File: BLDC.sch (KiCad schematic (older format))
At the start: 122 parts, among them J1 436500513, J2 436500313, J3 TC2030-MCP-NL, J4 436500513, U0 LSM6DS3US, U12 MCP9808, U13 AS5047D-ATSM, U17 INA250, U18 INA250, U19 INA250, U2 LM5166, U3 TLV702, U4 LM5166, U5 DRV8312, U6 ISL32458E, U7 SN74LVC1G66DCKR, U9 STM32F405RG

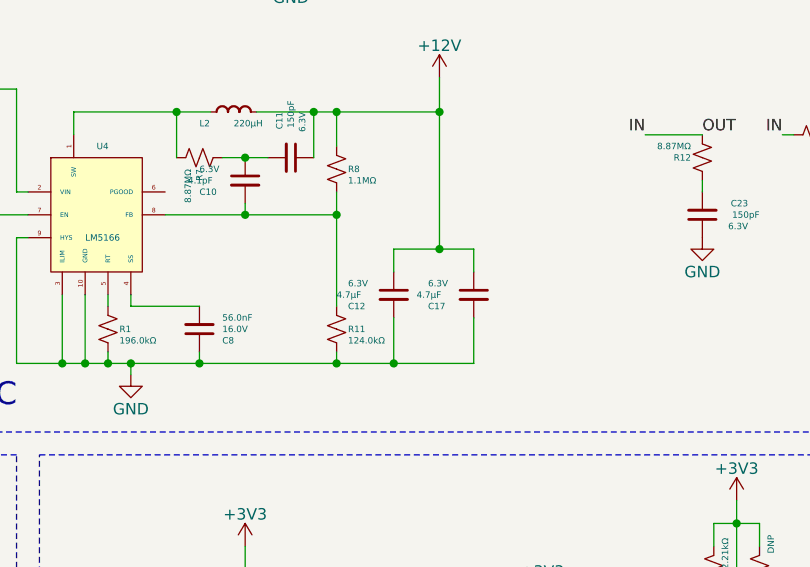
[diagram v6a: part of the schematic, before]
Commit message: Added ground pour in bottom layer for thermal dissipation and current return
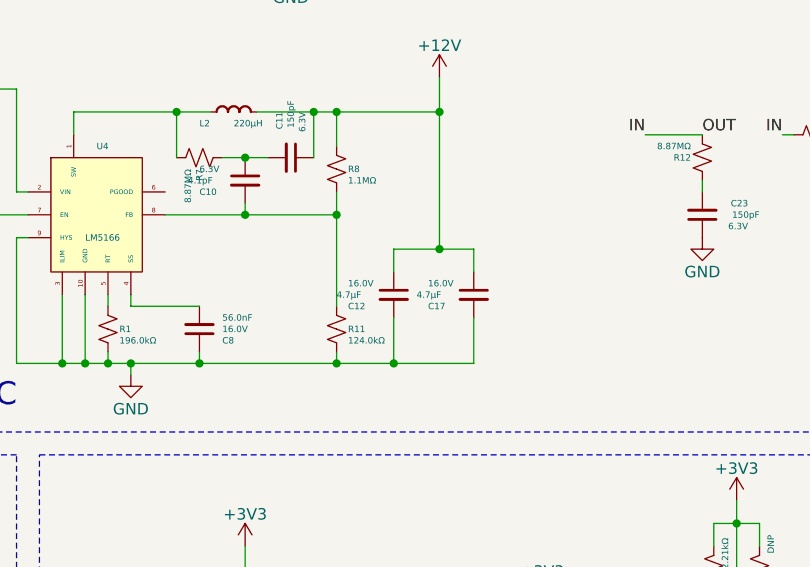
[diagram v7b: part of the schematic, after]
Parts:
- C12, C17: footprint Capacitor_SMD:C_1206_3216Metric -> Capacitor_SMD:C_0805_2012Metric; Maximum Voltage 6.3V -> 16.0V
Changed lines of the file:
@@
 EESchema Schematic File Version 5
 LIBS:BLDC-cache
-EELAYER 29 0
+EELAYER 30 0
 EELAYER END
 $Descr A3 16535 11693
@@
 F 0 "C12" H 8650 3850 28  0000 L CNN
 F 1 "4.7μF" H 8600 3900 28  0000 L CNN
-F 2 "Capacitor_SMD:C_1206_3216Metric" H 8850 3900 60  0001 C CNN
+F 2 "Capacitor_SMD:C_0805_2012Metric" H 8850 3900 60  0001 C CNN
 F 3 "" H 8850 3900 60  0001 C CNN
 F 4 "4.7μF" H 8850 3900 60  0001 C CNN "Capacitance"
 F 5 "40.0%" H 8850 3900 60  0001 C CNN "Tolerance"
-F 6 "6.3V" H 8650 3950 28  0000 L CNN "Maximum Voltage"
+F 6 "16.0V" H 8650 3950 28  0000 L CNN "Maximum Voltage"
 	1    8850 3900
 	1    0    0    -1
@@
 F 0 "C17" H 9000 3850 28  0000 L CNN
 F 1 "4.7μF" H 8950 3900 28  0000 L CNN
-F 2 "Capacitor_SMD:C_1206_3216Metric" H 9200 3900 60  0001 C CNN
+F 2 "Capacitor_SMD:C_0805_2012Metric" H 9200 3900 60  0001 C CNN
 F 3 "" H 9200 3900 60  0001 C CNN
 F 4 "4.7μF" H 9200 3900 60  0001 C CNN "Capacitance"
 F 5 "40.0%" H 9200 3900 60  0001 C CNN "Tolerance"
-F 6 "6.3V" H 9000 3950 28  0000 L CNN "Maximum Voltage"
+F 6 "16.0V" H 9000 3950 28  0000 L CNN "Maximum Voltage"
 	1    9200 3900
 	1    0    0    -1

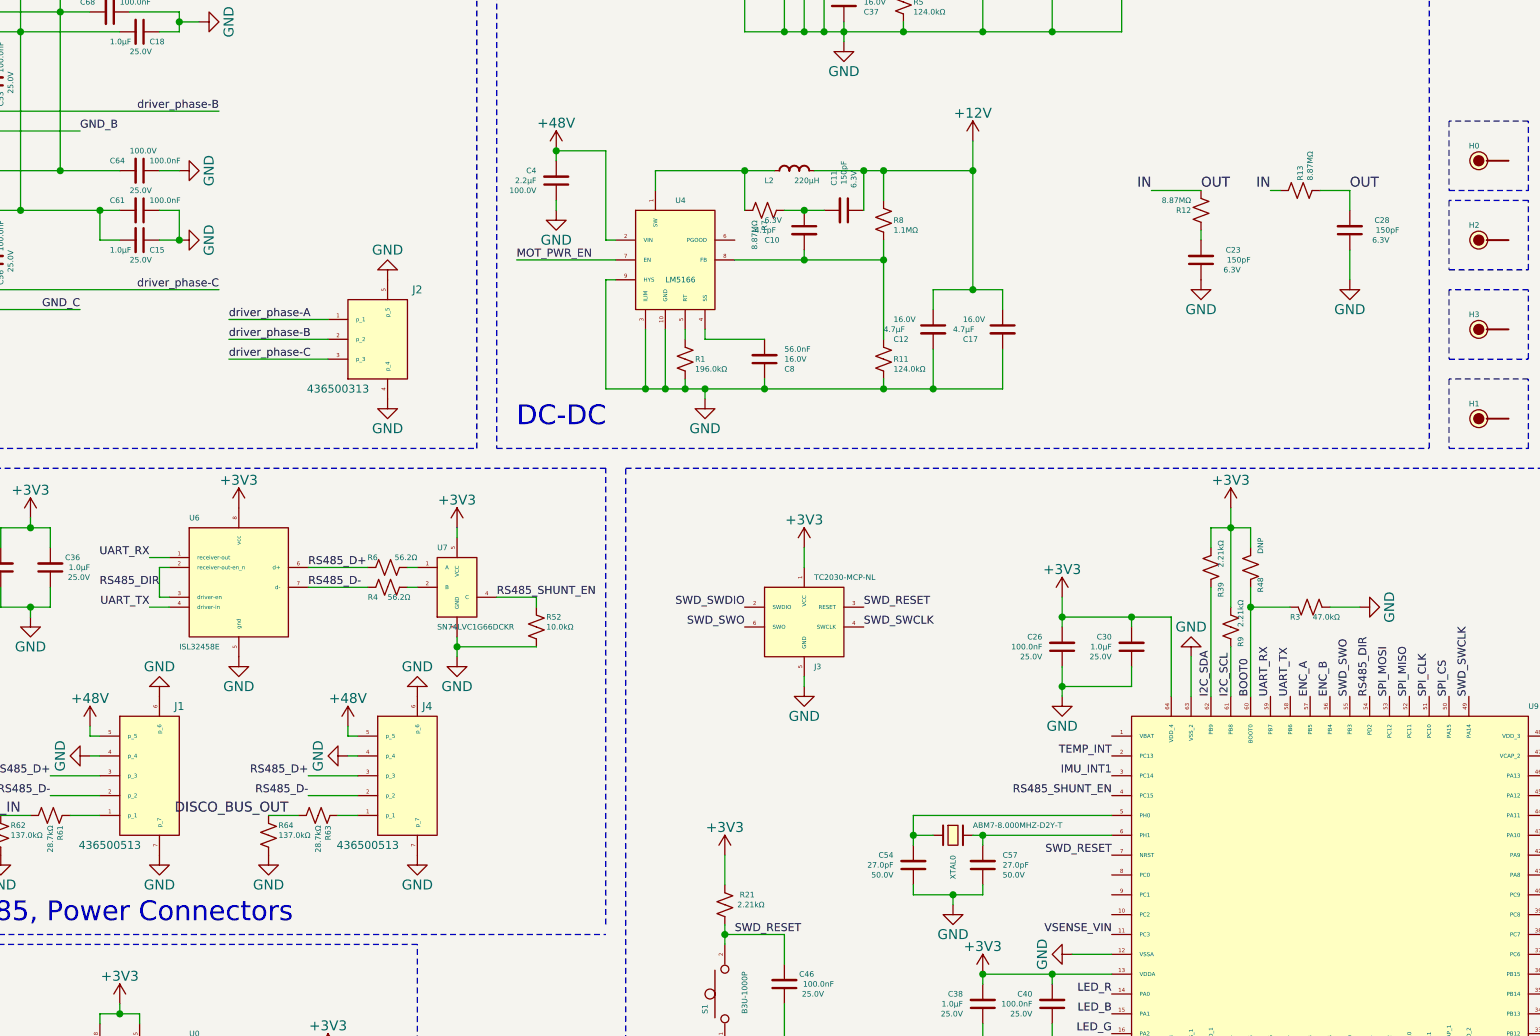
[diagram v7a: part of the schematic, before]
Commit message: Changed J1 connector to through hole and moved to middle of PCB
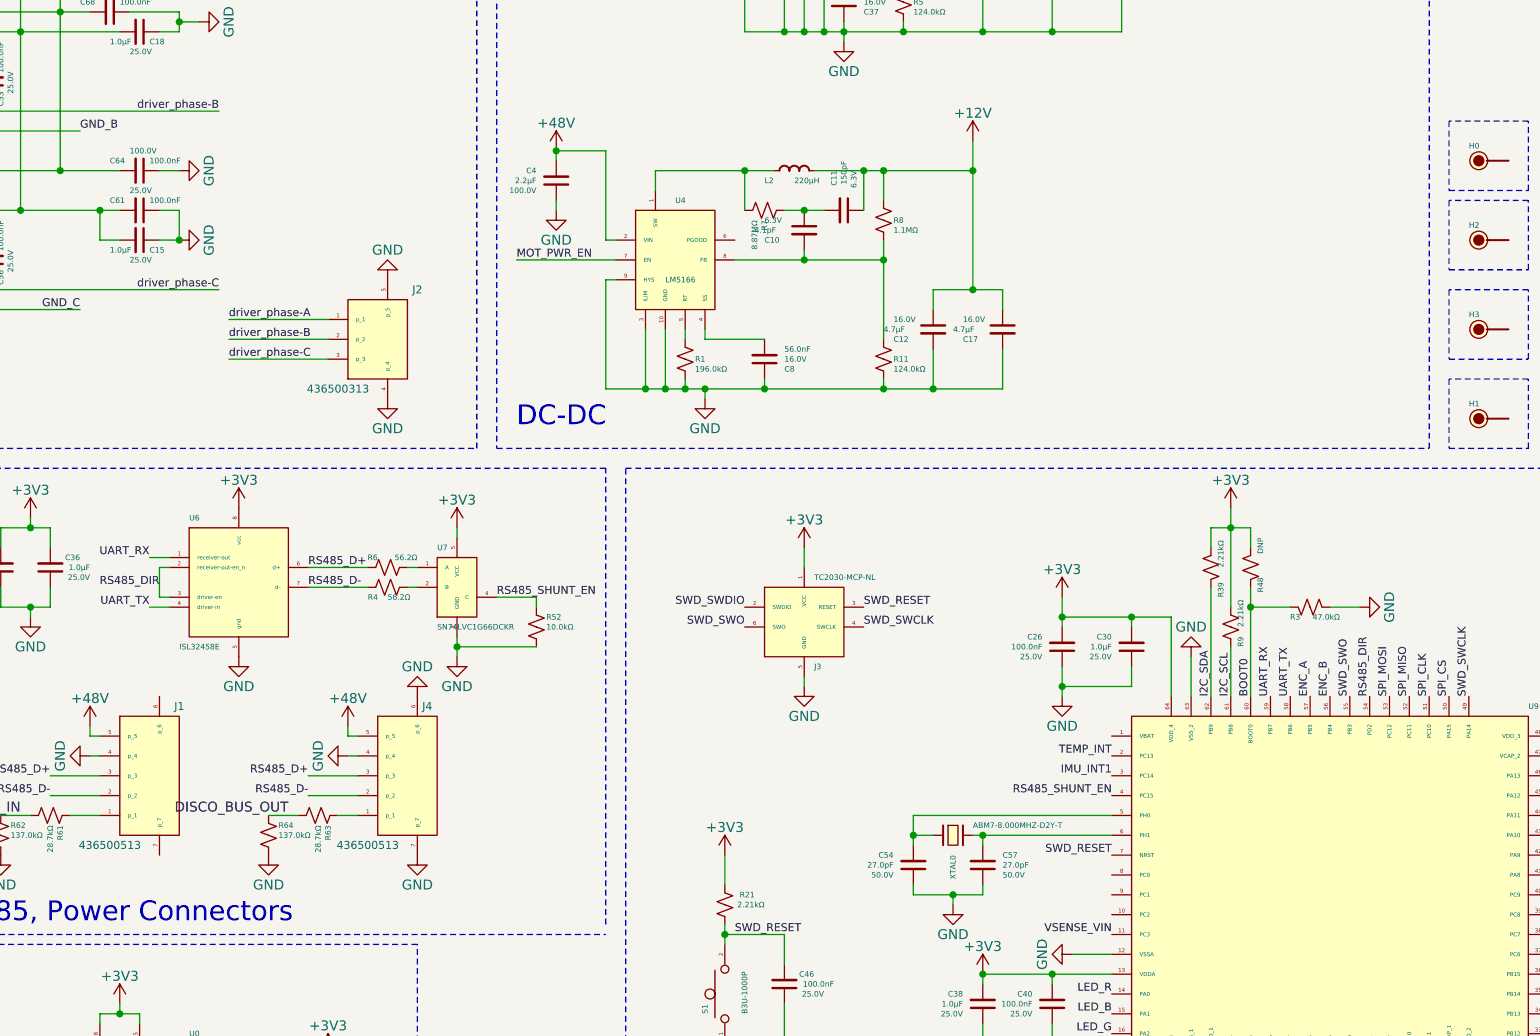
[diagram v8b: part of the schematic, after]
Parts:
- removed C23, C28: 150pF, Capacitor_SMD:C_0805_2012Metric, symbol Device:C_Small
- removed R12, R13: 8.87MΩ, Resistor_SMD:R_0805_2012Metric, symbol Device:R_Small_US
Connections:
- net GND: no longer J1.6 (p_6), J1.7 (p_7)
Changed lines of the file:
@@
-$EndComp
-$Comp
-L power:GND #PWR090
-U 1 1 5BCC0025
-P 4950 6550
-F 0 "#PWR090" H 4950 6300 50  0001 C CNN
-F 1 "GND" H 4950 6400 50  0000 C CNN
-F 2 "" H 4950 6550 50  0001 C CNN
-F 3 "" H 4950 6550 50  0001 C CNN
-	1    4950 6550
-	1    0    0    -1
 $EndComp
 $Comp
@@
 F 3 "" H 6250 5750 50  0001 C CNN
 	1    6250 5750
-	-1   0    0    1
-$EndComp
-$Comp
-L power:GND #PWR087
-U 1 1 5BCBFA49
-P 4950 5750
-F 0 "#PWR087" H 4950 5500 50  0001 C CNN
-F 1 "GND" H 4950 5600 50  0000 C CNN
-F 2 "" H 4950 5750 50  0001 C CNN
-F 3 "" H 4950 5750 50  0001 C CNN
-	1    4950 5750
 	-1   0    0    1
 $EndComp
@@
 $EndComp
 $Comp
-L Device:R_Small_US R12
-U 1 1 5D4F3434
-P 10200 3300
-F 0 "R12" H 10250 3300 28  0000 L CNN
-F 1 "8.87MΩ" H 10250 3250 28  0000 L CNN
-F 2 "Resistor_SMD:R_0805_2012Metric" H 10200 3300 60  0001 C CNN
-F 3 "" H 10200 3300 60  0001 C CNN
-F 4 "8870000.0ohm" H 10200 3300 60  0001 C CNN "Resistance"
-F 5 "0.1%" H 10200 3300 60  0001 C CNN "Tolerance"
-F 6 "0.125W" H 10200 3300 60  0001 C CNN "Maximum Power"
-	1    10200 3300
-	-1   0    0    1
-$EndComp
-$Comp
-L Device:C_Small C23
-U 1 1 5D4F868D
-P 10200 3550
-F 0 "C23" H 10000 3500 28  0000 L CNN
-F 1 "150pF" H 9950 3550 28  0000 L CNN
-F 2 "Capacitor_SMD:C_0805_2012Metric" H 10200 3550 60  0001 C CNN
-F 3 "" H 10200 3550 60  0001 C CNN
-F 4 "150pF" H 10200 3550 60  0001 C CNN "Capacitance"
-F 5 "40.0%" H 10200 3550 60  0001 C CNN "Tolerance"
-F 6 "6.3V" H 10000 3600 28  0000 L CNN "Maximum Voltage"
-	1    10200 3550
-	-1   0    0    1
-$EndComp
-Wire Wire Line
-	9950 3200 10200 3200
-Wire Wire Line
-	10200 3400 10200 3450
-$Comp
-L power:GND #PWR0107
-U 1 1 5D4F90AD
-P 10200 3650
-F 0 "#PWR0107" H 10200 3400 50  0001 C CNN
-F 1 "GND" H 10200 3500 50  0000 C CNN
-F 2 "" H 10200 3650 50  0001 C CNN
-F 3 "" H 10200 3650 50  0001 C CNN
-	1    10200 3650
-	1    0    0    -1
-$EndComp
-$Comp
-L Device:R_Small_US R13
-U 1 1 5D4F9647
-P 10700 3200
-F 0 "R13" H 10750 3200 28  0000 L CNN
-F 1 "8.87MΩ" H 10750 3150 28  0000 L CNN
-F 2 "Resistor_SMD:R_0805_2012Metric" H 10700 3200 60  0001 C CNN
-F 3 "" H 10700 3200 60  0001 C CNN
-F 4 "8870000.0ohm" H 10700 3200 60  0001 C CNN "Resistance"
-F 5 "0.1%" H 10700 3200 60  0001 C CNN "Tolerance"
-F 6 "0.125W" H 10700 3200 60  0001 C CNN "Maximum Power"
-	1    10700 3200
-	0    -1   -1   0
-$EndComp
-$Comp
-L Device:C_Small C28
-U 1 1 5D4F9CC5
-P 10950 3400
-F 0 "C28" H 10750 3350 28  0000 L CNN
-F 1 "150pF" H 10700 3400 28  0000 L CNN
-F 2 "Capacitor_SMD:C_0805_2012Metric" H 10950 3400 60  0001 C CNN
-F 3 "" H 10950 3400 60  0001 C CNN
-F 4 "150pF" H 10950 3400 60  0001 C CNN "Capacitance"
-F 5 "40.0%" H 10950 3400 60  0001 C CNN "Tolerance"
-F 6 "6.3V" H 10750 3450 28  0000 L CNN "Maximum Voltage"
-	1    10950 3400
-	-1   0    0    1
-$EndComp
-Wire Wire Line
-	10800 3200 10950 3200
-Wire Wire Line
-	10950 3200 10950 3300
-$Comp
-L power:GND #PWR0108
-U 1 1 5D4FA116
-P 10950 3650
-F 0 "#PWR0108" H 10950 3400 50  0001 C CNN
-F 1 "GND" H 10950 3500 50  0000 C CNN
-F 2 "" H 10950 3650 50  0001 C CNN
-F 3 "" H 10950 3650 50  0001 C CNN
-	1    10950 3650
-	1    0    0    -1
-$EndComp
-Wire Wire Line
-	10950 3650 10950 3500
-Wire Wire Line
-	10550 3200 10600 3200
-Text Label 10550 3200 2    50   ~ 0
-IN
-Text Label 10950 3200 0    50   ~ 0
-OUT
-Text Label 10200 3200 0    50   ~ 0
-OUT
-Text Label 9950 3200 2    50   ~ 0
-IN
-$Comp
 L Device:CP_Small C9
